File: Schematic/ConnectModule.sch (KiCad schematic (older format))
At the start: 26 parts, among them J1 Solar panel, J2 Battery, J3 LOAD, J4 Temperature, J5 Buck1_IN, J6 Buck1_OUT, J7 Buck2_IN, J8 Buck2_OUT, U1 ACS712module, U3 XL4016_DC-DC_module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

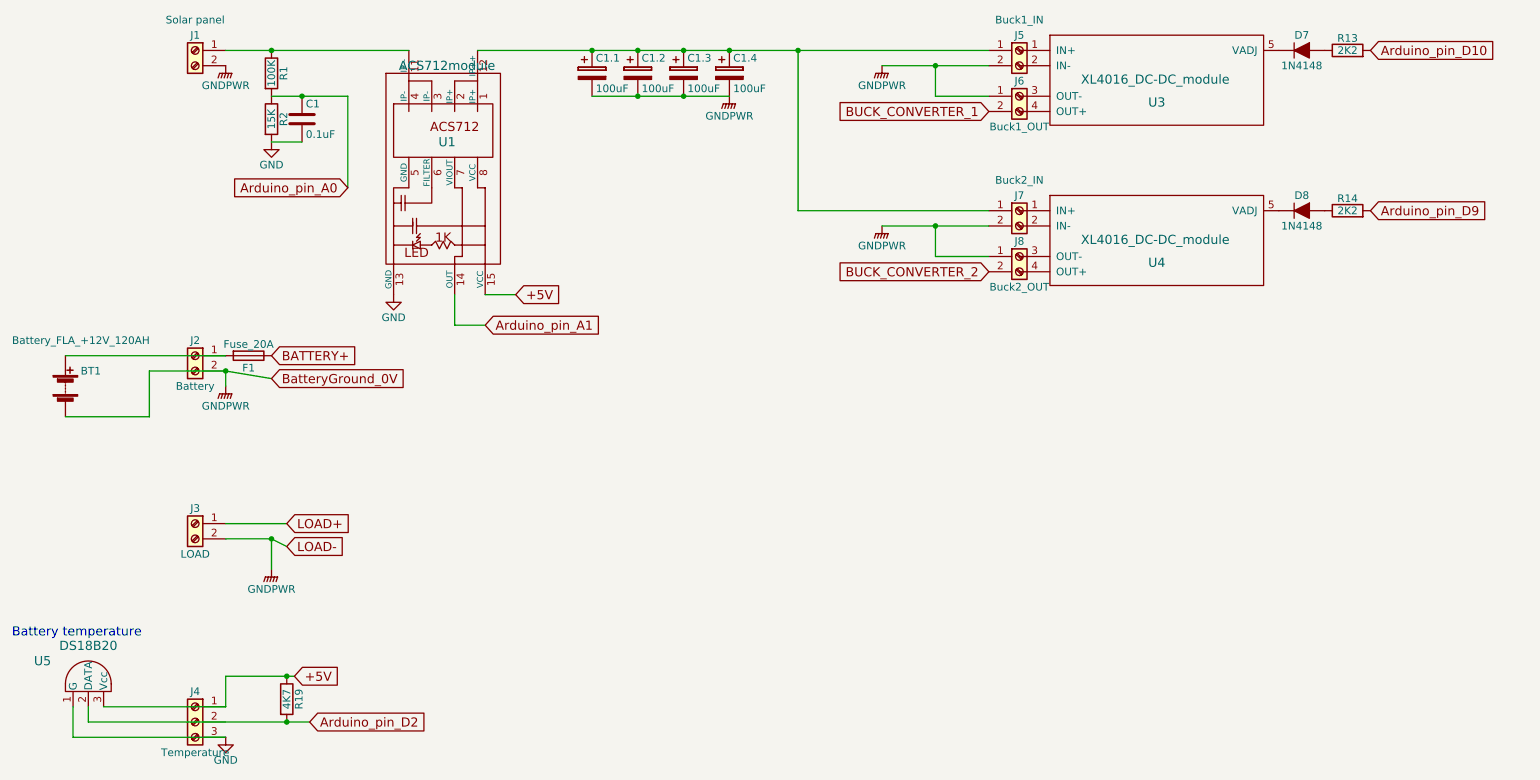
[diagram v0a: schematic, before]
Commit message: Added TVS diode to connect module
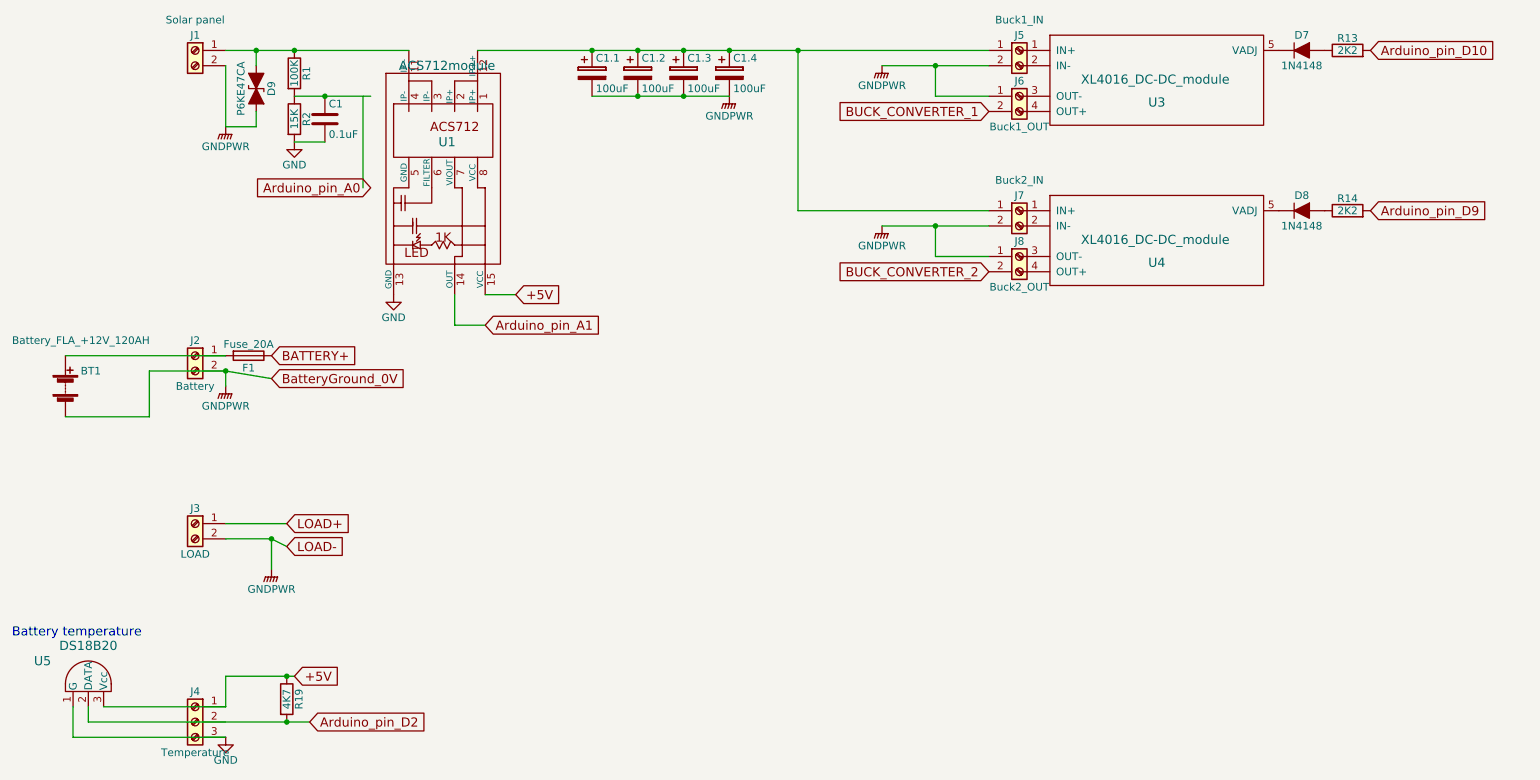
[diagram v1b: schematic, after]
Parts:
- added D9: P6KE47CA, symbol D_TVS_ALT
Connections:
- wire segments 34 -> 52
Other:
- moved on the sheet: C1, R1, R2
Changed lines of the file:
@@
 $EndComp
 $Comp
-L GNDPWR #PWR1
+L GNDPWR #PWR3
 U 1 1 5A5727E5
-P 2000 1700
-F 0 "#PWR1" H 2000 1500 50  0001 C CNN
-F 1 "GNDPWR" H 2000 1570 50  0000 C CNN
-F 2 "" H 2000 1650 50  0001 C CNN
-F 3 "" H 2000 1650 50  0001 C CNN
-	1    2000 1700
+P 2000 2100
+F 0 "#PWR3" H 2000 1900 50  0001 C CNN
+F 1 "GNDPWR" H 2000 1970 50  0000 C CNN
+F 2 "" H 2000 2050 50  0001 C CNN
+F 3 "" H 2000 2050 50  0001 C CNN
+	1    2000 2100
 	1    0    0    -1
 $EndComp
@@
 L R R1
 U 1 1 5A57281B
-P 2300 1750
-F 0 "R1" V 2380 1750 50  0000 C CNN
-F 1 "100K" V 2300 1750 50  0000 C CNN
-F 2 "" V 2230 1750 50  0001 C CNN
-F 3 "" H 2300 1750 50  0001 C CNN
-	1    2300 1750
+P 2450 1750
+F 0 "R1" V 2530 1750 50  0000 C CNN
+F 1 "100K" V 2450 1750 50  0000 C CNN
+F 2 "" V 2380 1750 50  0001 C CNN
+F 3 "" H 2450 1750 50  0001 C CNN
+	1    2450 1750
 	1    0    0    -1
 $EndComp
@@
 L R R2
 U 1 1 5A57283E
-P 2300 2050
-F 0 "R2" V 2380 2050 50  0000 C CNN
-F 1 "15K" V 2300 2050 50  0000 C CNN
-F 2 "" V 2230 2050 50  0001 C CNN
-F 3 "" H 2300 2050 50  0001 C CNN
-	1    2300 2050
+P 2450 2050
+F 0 "R2" V 2530 2050 50  0000 C CNN
+F 1 "15K" V 2450 2050 50  0000 C CNN
+F 2 "" V 2380 2050 50  0001 C CNN
+F 3 "" H 2450 2050 50  0001 C CNN
+	1    2450 2050
 	1    0    0    -1
 $EndComp
@@
 L C C1
 U 1 1 5A57286F
-P 2500 2050
-F 0 "C1" H 2525 2150 50  0000 L CNN
-F 1 "0.1uF" H 2525 1950 50  0000 L CNN
-F 2 "" H 2538 1900 50  0001 C CNN
-F 3 "" H 2500 2050 50  0001 C CNN
-	1    2500 2050
-	1    0    0    -1
-$EndComp
-Wire Wire Line
-	2300 1900 2800 1900
-Wire Wire Line
-	2000 1600 3200 1600
+P 2650 2050
+F 0 "C1" H 2675 2150 50  0000 L CNN
+F 1 "0.1uF" H 2675 1950 50  0000 L CNN
+F 2 "" H 2688 1900 50  0001 C CNN
+F 3 "" H 2650 2050 50  0001 C CNN
+	1    2650 2050
+	1    0    0    -1
+$EndComp
+Wire Wire Line
+	2450 1900 2650 1900
+Wire Wire Line
+	2650 1900 2950 1900
+Wire Wire Line
+	2000 1600 2200 1600
+Wire Wire Line
+	2200 1600 2450 1600
+Wire Wire Line
+	2450 1600 3200 1600
 $Comp
 L GND #PWR4
 U 1 1 5A57292E
-P 2300 2200
-F 0 "#PWR4" H 2300 1950 50  0001 C CNN
-F 1 "GND" H 2300 2050 50  0000 C CNN
-F 2 "" H 2300 2200 50  0001 C CNN
-F 3 "" H 2300 2200 50  0001 C CNN
-	1    2300 2200
-	1    0    0    -1
-$EndComp
-Wire Wire Line
-	2500 2200 2300 2200
-Connection ~ 2500 1900
+P 2450 2200
+F 0 "#PWR4" H 2450 1950 50  0001 C CNN
+F 1 "GND" H 2450 2050 50  0000 C CNN
+F 2 "" H 2450 2200 50  0001 C CNN
+F 3 "" H 2450 2200 50  0001 C CNN
+	1    2450 2200
+	1    0    0    -1
+$EndComp
+Wire Wire Line
+	2650 2200 2450 2200
+Connection ~ 2650 1900
 Wire Wire Line
 	2000 3700 2000 3800
@@
 	1    0    0    -1
 $EndComp
-Connection ~ 2300 1600
 Connection ~ 5000 1600
 Connection ~ 5300 1600
 Wire Wire Line
-	4400 1900 5300 1900
+	4400 1900 4700 1900
+Wire Wire Line
+	4700 1900 5000 1900
+Wire Wire Line
+	5000 1900 5300 1900
 Connection ~ 4700 1900
 Connection ~ 5000 1900
 $Comp
-L GNDPWR #PWR3
+L GNDPWR #PWR2
 U 1 1 5A57411F
 P 5300 1900
-F 0 "#PWR3" H 5300 1700 50  0001 C CNN
+F 0 "#PWR2" H 5300 1700 50  0001 C CNN
 F 1 "GNDPWR" H 5300 1770 50  0000 C CNN
 F 2 "" H 5300 1850 50  0001 C CNN
@@
 Text GLabel 3700 3400 2    60   Input ~ 0
 Arduino_pin_A1
-Text GLabel 2800 2500 0    60   Input ~ 0
+Text GLabel 2950 2500 0    60   Input ~ 0
 Arduino_pin_A0
 Wire Wire Line
-	2800 1900 2800 2500
+	2900 1900 2900 2500
 $Comp
 L Fuse F1
@@
 Connection ~ 2000 3700
 Wire Wire Line
-	3650 1600 7000 1600
+	3650 1600 4400 1600
+Wire Wire Line
+	4400 1600 4700 1600
+Wire Wire Line
+	4700 1600 5000 1600
+Wire Wire Line
+	5000 1600 5300 1600
+Wire Wire Line
+	5300 1600 5750 1600
+Wire Wire Line
+	5750 1600 7000 1600
 Connection ~ 4700 1600
 Connection ~ 4400 1600
@@
 Connection ~ 5750 1600
 $Comp
-L GNDPWR #PWR2
+L GNDPWR #PWR1
 U 1 1 5AC8C6DA
 P 6300 1700
-F 0 "#PWR2" H 6300 1500 50  0001 C CNN
+F 0 "#PWR1" H 6300 1500 50  0001 C CNN
 F 1 "GNDPWR" H 6300 1570 50  0000 C CNN
 F 2 "" H 6300 1650 50  0001 C CNN
@@
 $EndComp
 Wire Wire Line
-	7000 1700 6300 1700
+	6300 1700 6650 1700
+Wire Wire Line
+	6650 1700 7000 1700
 Wire Wire Line
 	7000 1900 6650 1900
@@
 $EndComp
 Wire Wire Line
-	7000 2750 6300 2750
+	6300 2750 6650 2750
+Wire Wire Line
+	6650 2750 7000 2750
 Wire Wire Line
 	6650 2950 6650 2750
@@
 Arduino_pin_D2
 Wire Wire Line
-	1100 6000 2550 6000
+	1100 6000 2400 6000
+Wire Wire Line
+	2400 6000 2550 6000
 $Comp
 L GND #PWR9
@@
 $EndComp
 Wire Wire Line
-	2000 5700 2450 5700
-Wire Wire Line
-	2000 5700 2000 5900
+	2000 5700 2400 5700
+Wire Wire Line
+	2400 5700 2450 5700
+Wire Wire Line
+	2000 5900 2000 5700
 Connection ~ 2400 5700
 Connection ~ 2400 6000
+$Comp
+L D_TVS_ALT D9
+U 1 1 5AC7F9EE
+P 2200 1850
+F 0 "D9" H 2200 1950 50  0000 C CNN
+F 1 "P6KE47CA" H 2200 1750 50  0000 C CNN
+F 2 "" H 2200 1850 50  0001 C CNN
+F 3 "" H 2200 1850 50  0001 C CNN
+	1    2200 1850
+	0    1    1    0
+$EndComp
+Connection ~ 2450 1600
+Wire Wire Line
+	2200 2100 2000 2100
+Wire Wire Line
+	2000 2100 2000 1700
+Wire Wire Line
+	2200 2000 2200 2100
+Wire Wire Line
+	2200 1700 2200 1600
+Connection ~ 2200 1600
 $EndSCHEMATC

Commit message: added BOM, started Fritzing prototype diagram, minor layout changes in KiCad
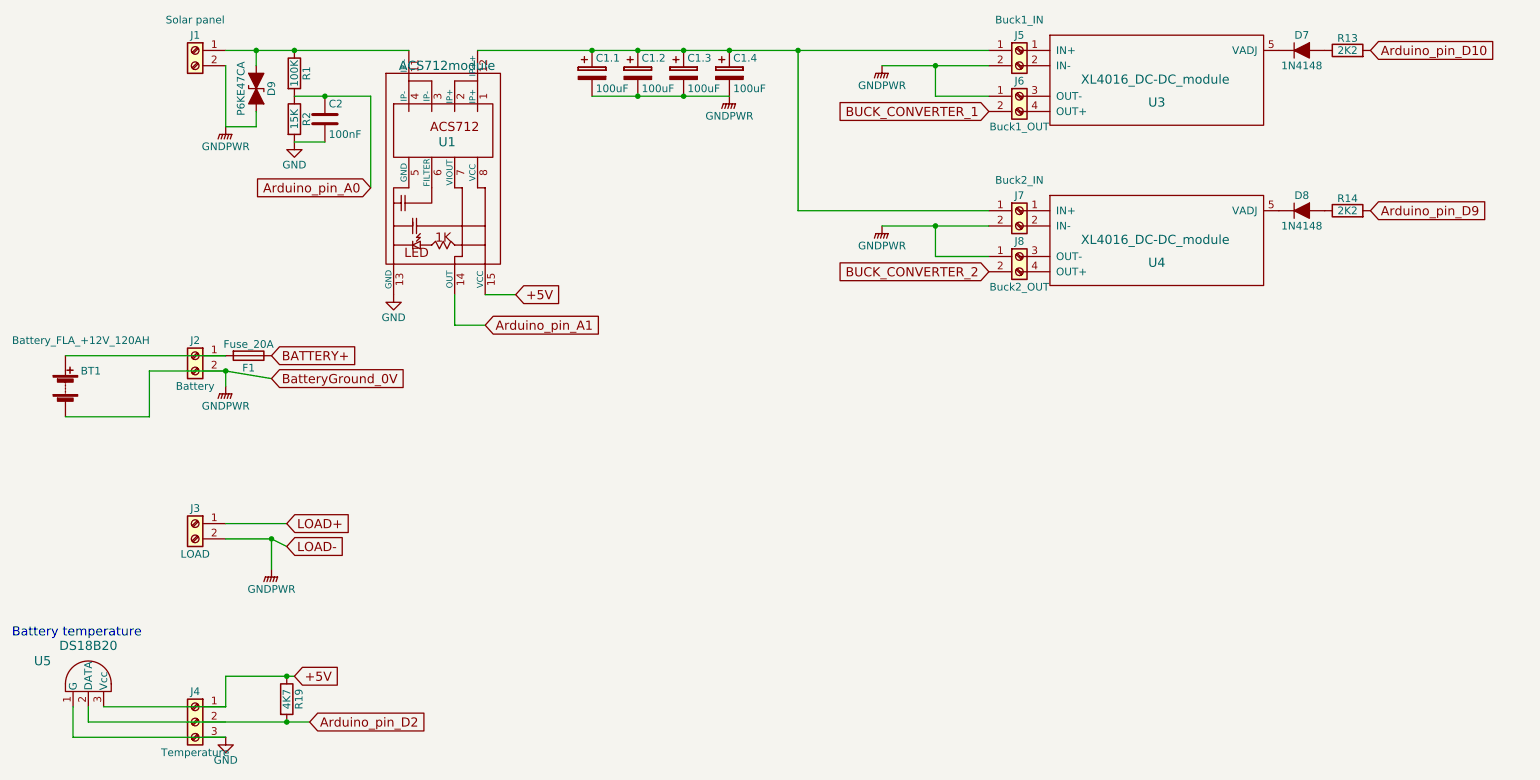
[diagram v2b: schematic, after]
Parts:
- C2: renamed from C1; value 0.1uF -> 100nF
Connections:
- wire segments 52 -> 38
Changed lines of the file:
@@
 $EndComp
 $Comp
-L GNDPWR #PWR3
+L GNDPWR #PWR01
 U 1 1 5A5727E5
 P 2000 2100
-F 0 "#PWR3" H 2000 1900 50  0001 C CNN
+F 0 "#PWR01" H 2000 1900 50  0001 C CNN
 F 1 "GNDPWR" H 2000 1970 50  0000 C CNN
 F 2 "" H 2000 2050 50  0001 C CNN
@@
 $EndComp
 $Comp
-L GNDPWR #PWR7
+L GNDPWR #PWR02
 U 1 1 5A572803
 P 2000 3800
-F 0 "#PWR7" H 2000 3600 50  0001 C CNN
+F 0 "#PWR02" H 2000 3600 50  0001 C CNN
 F 1 "GNDPWR" H 2000 3670 50  0000 C CNN
 F 2 "" H 2000 3750 50  0001 C CNN
@@
 $EndComp
 $Comp
-L C C1
+L C C2
 U 1 1 5A57286F
 P 2650 2050
-F 0 "C1" H 2675 2150 50  0000 L CNN
-F 1 "0.1uF" H 2675 1950 50  0000 L CNN
+F 0 "C2" H 2675 2150 50  0000 L CNN
+F 1 "100nF" H 2675 1950 50  0000 L CNN
 F 2 "" H 2688 1900 50  0001 C CNN
 F 3 "" H 2650 2050 50  0001 C CNN
@@
 $EndComp
 Wire Wire Line
-	2450 1900 2650 1900
-Wire Wire Line
-	2650 1900 2950 1900
-Wire Wire Line
-	2000 1600 2200 1600
-Wire Wire Line
-	2200 1600 2450 1600
-Wire Wire Line
-	2450 1600 3200 1600
-$Comp
-L GND #PWR4
+	2450 1900 2950 1900
+Wire Wire Line
+	2000 1600 3200 1600
+$Comp
+L GND #PWR03
 U 1 1 5A57292E
 P 2450 2200
-F 0 "#PWR4" H 2450 1950 50  0001 C CNN
+F 0 "#PWR03" H 2450 1950 50  0001 C CNN
 F 1 "GND" H 2450 2050 50  0000 C CNN
 F 2 "" H 2450 2200 50  0001 C CNN
@@
 	2300 4800 2300 5000
 $Comp
-L GNDPWR #PWR8
+L GNDPWR #PWR04
 U 1 1 5A573362
 P 2300 5000
-F 0 "#PWR8" H 2300 4800 50  0001 C CNN
+F 0 "#PWR04" H 2300 4800 50  0001 C CNN
 F 1 "GNDPWR" H 2300 4870 50  0000 C CNN
 F 2 "" H 2300 4950 50  0001 C CNN
@@
 Connection ~ 5300 1600
 Wire Wire Line
-	4400 1900 4700 1900
-Wire Wire Line
-	4700 1900 5000 1900
-Wire Wire Line
-	5000 1900 5300 1900
+	4400 1900 5300 1900
 Connection ~ 4700 1900
 Connection ~ 5000 1900
 $Comp
-L GNDPWR #PWR2
+L GNDPWR #PWR05
 U 1 1 5A57411F
 P 5300 1900
-F 0 "#PWR2" H 5300 1700 50  0001 C CNN
+F 0 "#PWR05" H 5300 1700 50  0001 C CNN
 F 1 "GNDPWR" H 5300 1770 50  0000 C CNN
 F 2 "" H 5300 1850 50  0001 C CNN
@@
 $EndComp
 $Comp
-L GND #PWR6
+L GND #PWR06
 U 1 1 5A577A94
 P 3100 3200
-F 0 "#PWR6" H 3100 2950 50  0001 C CNN
+F 0 "#PWR06" H 3100 2950 50  0001 C CNN
 F 1 "GND" H 3100 3050 50  0000 C CNN
 F 2 "" H 3100 3200 50  0001 C CNN
@@
 Arduino_pin_A0
 Wire Wire Line
-	2900 1900 2900 2500
+	2950 1900 2950 2500
 $Comp
 L Fuse F1
@@
 Connection ~ 2000 3700
 Wire Wire Line
-	3650 1600 4400 1600
-Wire Wire Line
-	4400 1600 4700 1600
-Wire Wire Line
-	4700 1600 5000 1600
-Wire Wire Line
-	5000 1600 5300 1600
-Wire Wire Line
-	5300 1600 5750 1600
-Wire Wire Line
-	5750 1600 7000 1600
+	3650 1600 7000 1600
 Connection ~ 4700 1600
 Connection ~ 4400 1600
@@
 Connection ~ 5750 1600
 $Comp
-L GNDPWR #PWR1
+L GNDPWR #PWR07
 U 1 1 5AC8C6DA
 P 6300 1700
-F 0 "#PWR1" H 6300 1500 50  0001 C CNN
+F 0 "#PWR07" H 6300 1500 50  0001 C CNN
 F 1 "GNDPWR" H 6300 1570 50  0000 C CNN
 F 2 "" H 6300 1650 50  0001 C CNN
@@
 $EndComp
 Wire Wire Line
-	6300 1700 6650 1700
-Wire Wire Line
-	6650 1700 7000 1700
+	6300 1700 7000 1700
 Wire Wire Line
 	7000 1900 6650 1900
@@
 Connection ~ 6650 1700
 $Comp
-L GNDPWR #PWR5
+L GNDPWR #PWR08
 U 1 1 5AC8C7C0
 P 6300 2750
-F 0 "#PWR5" H 6300 2550 50  0001 C CNN
+F 0 "#PWR08" H 6300 2550 50  0001 C CNN
 F 1 "GNDPWR" H 6300 2620 50  0000 C CNN
 F 2 "" H 6300 2700 50  0001 C CNN
@@
 $EndComp
 Wire Wire Line
-	6300 2750 6650 2750
-Wire Wire Line
-	6650 2750 7000 2750
+	6300 2750 7000 2750
 Wire Wire Line
 	6650 2950 6650 2750
@@
 Arduino_pin_D2
 Wire Wire Line
-	1100 6000 2400 6000
-Wire Wire Line
-	2400 6000 2550 6000
-$Comp
-L GND #PWR9
+	1100 6000 2550 6000
+$Comp
+L GND #PWR09
 U 1 1 5AC9172C
 P 2000 6100
-F 0 "#PWR9" H 2000 5850 50  0001 C CNN
+F 0 "#PWR09" H 2000 5850 50  0001 C CNN
 F 1 "GND" H 2000 5950 50  0000 C CNN
 F 2 "" H 2000 6100 50  0001 C CNN
@@
 $EndComp
 Wire Wire Line
-	2000 5700 2400 5700
-Wire Wire Line
-	2400 5700 2450 5700
+	2000 5700 2450 5700
 Wire Wire Line
 	2000 5900 2000 5700
